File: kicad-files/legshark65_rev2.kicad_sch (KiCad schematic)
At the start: 206 parts, among them J1 ARM JTAG, J2 X1224WRS-04-LPV01, J3 Conn_01x04, SW1 K2-1187SQ-A4SW-06, SW2 PCM12SMTR, T2 SM04B-SRSS-TB, U1 STM32F411CEU6, U2 MCP1700T-3302E/TT, U3 AT24C256C-SSHL-T, Y1 TAXM8M4RFDCET2T

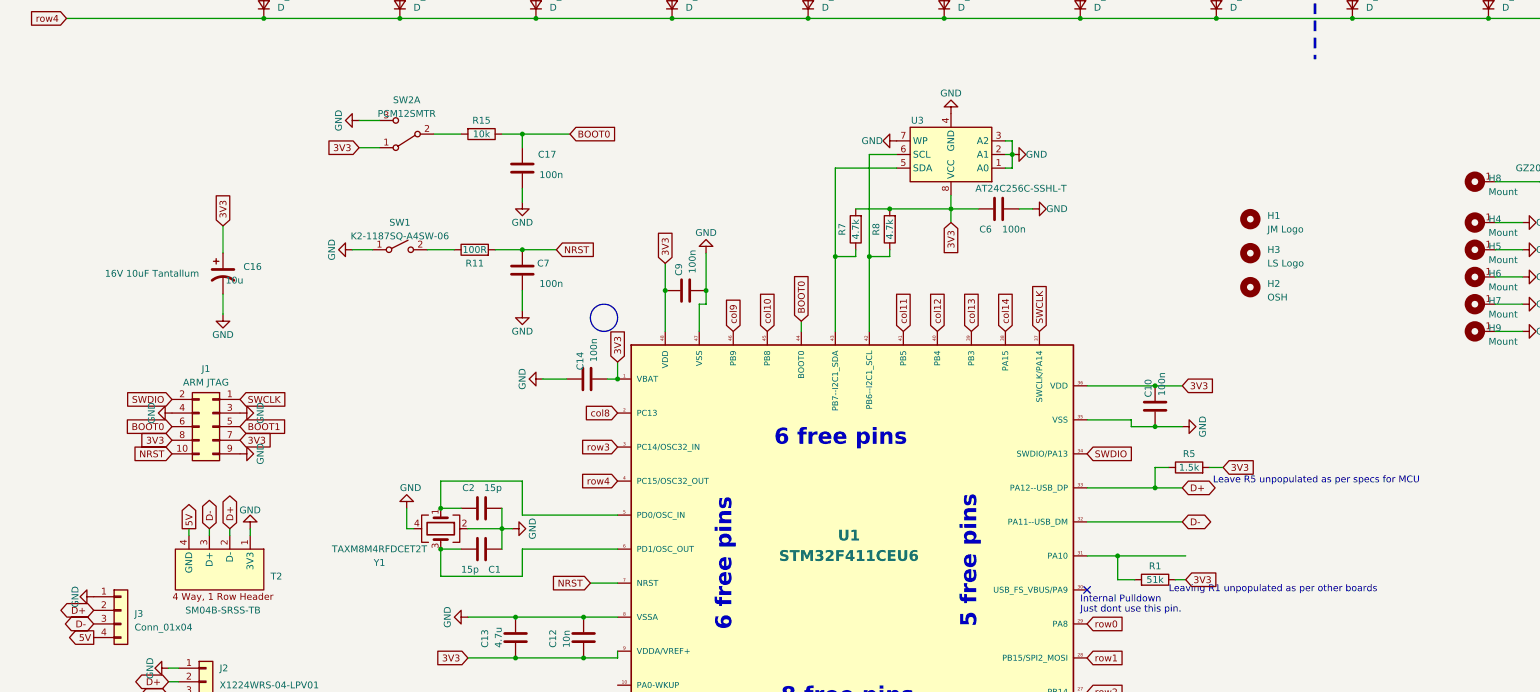
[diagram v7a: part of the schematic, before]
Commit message: Added power indicator LED
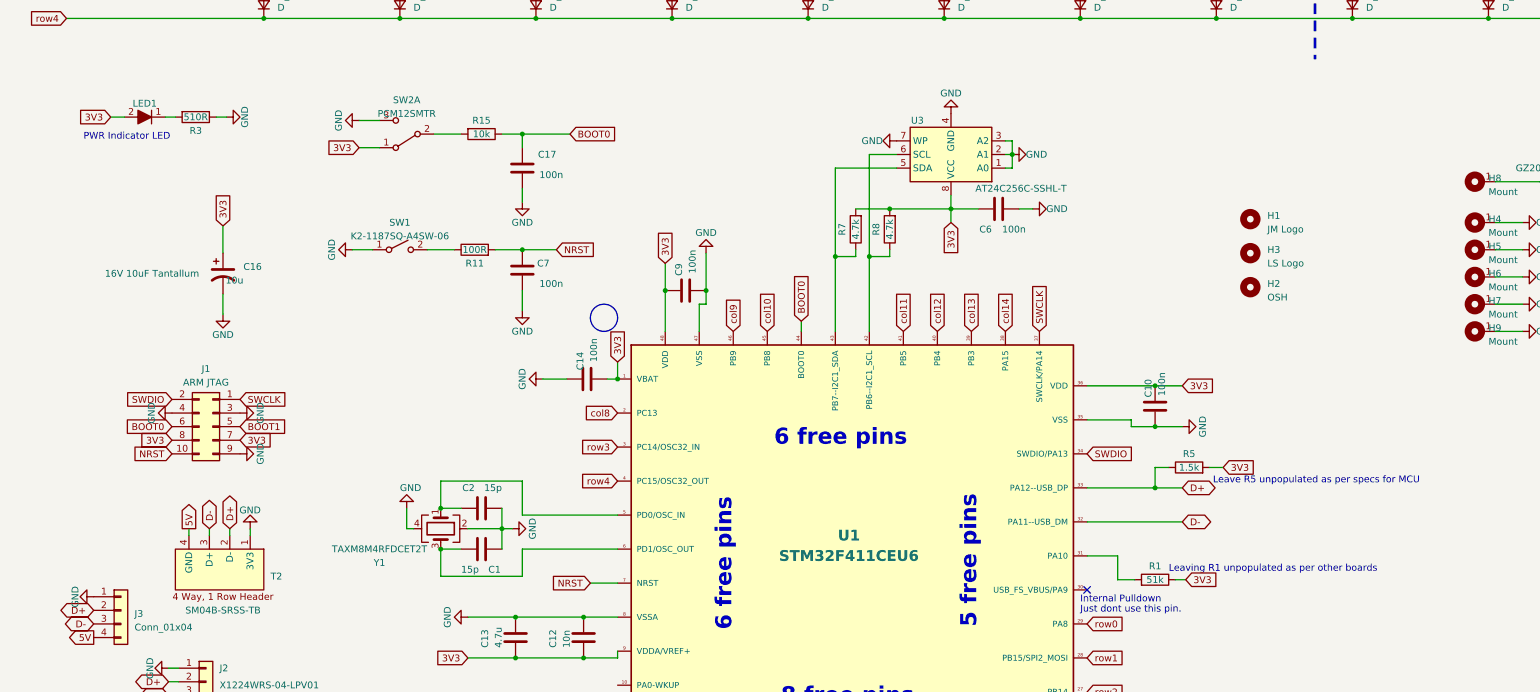
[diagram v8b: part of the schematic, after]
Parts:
- added LED1: ~, Legshark:LED_0603, symbol legshark_symbols:LED_0603
- added R3: 510R, Resistor_SMD:R_0402_1005Metric_Pad0.72x0.64mm_HandSolder, symbol Device:R
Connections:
- net 3V3: now also LED1.2
- net GND: now also R3.1
- new net: LED1.1, R3.2
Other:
- note added: "PWR Indicator LED"
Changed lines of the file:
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@@
   (junction (at 274.32 24.13) (diameter 0) (color 0 0 0 0)
   )
-  (junction (at 219.075 237.49) (diameter 0) (color 0 0 0 0)
-  )
   (junction (at 107.95 158.75) (diameter 0) (color 0 0 0 0)
   )
@@
     (stroke (width 0) (type default))
   )
-  (wire (pts (xy 219.075 237.49) (xy 231.775 237.49))
-    (stroke (width 0) (type default))
-  )
   (wire (pts (xy 135.89 111.76) (xy 161.29 111.76))
     (stroke (width 0) (type default))
@@
     (stroke (width 0) (type default))
   )
+  (wire (pts (xy 50.8 155.575) (xy 52.705 155.575))
+    (stroke (width 0) (type default))
+  )
   (wire (pts (xy 107.95 171.45) (xy 107.95 168.91))
     (stroke (width 0) (type default))
@@
     (stroke (width 0) (type default))
   )
+  (wire (pts (xy 31.115 155.575) (xy 33.655 155.575))
+    (stroke (width 0) (type default))
+  )
   (wire (pts (xy 299.72 100.33) (xy 299.72 74.93))
     (stroke (width 0) (type default))
@@
     (stroke (width 0) (type default))
   )
+  (wire (pts (xy 41.275 155.575) (xy 43.18 155.575))
+    (stroke (width 0) (type default))
+  )
   (wire (pts (xy 369.57 100.33) (xy 375.92 100.33))
     (stroke (width 0) (type default))
@@
     (effects (font (size 1.27 1.27)) (justify left bottom))
   )
+  (text "PWR Indicator LED" (at 26.035 160.02 0)
+    (effects (font (size 1.27 1.27)) (justify left bottom))
+  )
   (text "Leave R5 unpopulated as per specs for MCU" (at 236.855 224.155 0)
     (effects (font (size 1.27 1.27)) (justify left bottom))
@@
     (effects (font (size 1.27 1.27)) (justify left bottom))
   )
-  (text "Leaving R1 unpopulated as per other boards" (at 228.6 244.475 0)
+  (text "Leaving R1 unpopulated as per other boards" (at 228.6 240.665 0)
     (effects (font (size 1.27 1.27)) (justify left bottom))
   )
@@
     )
   )
+  (global_label "3V3" (shape input) (at 31.115 155.575 180) (fields_autoplaced)
+    (effects (font (size 1.27 1.27)) (justify right))
+    (property "Intersheetrefs" "${INTERSHEET_REFS}" (at 25.3558 155.575 0)
+      (effects (font (size 1.27 1.27)) (justify right) hide)
+    )
+  )
   (global_label "D-" (shape bidirectional) (at 41.91 263.525 180) (fields_autoplaced)
     (effects (font (size 1.27 1.27)) (justify right))
@@
     )
   )
+  (symbol (lib_id "legshark_symbols:LED_0603") (at 37.465 155.575 180) (unit 1)
+    (in_bom yes) (on_board yes) (dnp no)
+    (property "Reference" "LED1" (at 37.465 153.035 0)
+      (effects (font (size 1.27 1.27)))
+    )
+    (property "Value" "~" (at 38.735 156.845 0)
+      (effects (font (size 1.27 1.27)))
+    )
+    (property "Footprint" "Legshark:LED_0603" (at 38.735 156.845 0)
+      (effects (font (size 1.27 1.27)) hide)
+    )
+    (property "Datasheet" "" (at 38.735 156.845 0)
+      (effects (font (size 1.27 1.27)) hide)
+    )
+    (property "Specification" "Red 0603 SMD LED " (at 37.465 155.575 0)
+      (effects (font (size 1.27 1.27)) hide)
+    )
+    (pin "1")
+    (pin "2")
+    (instances
+      (project "legshark65_rev2"
+        (path "/2fcc1073-d3f4-43f9-b3b4-5cee13272705"
+          (reference "LED1") (unit 1)
+        )
+      )
+    )
+  )
   (symbol (lib_id "MX_Alps_Hybrid:MX-NoLED") (at 162.56 25.4 0) (unit 1)
     (in_bom yes) (on_board yes) (dnp no)
@@
     )
   )
+  (symbol (lib_id "power:GND") (at 52.705 155.575 90) (unit 1)
+    (in_bom yes) (on_board yes) (dnp no)
+    (property "Reference" "#PWR036" (at 59.055 155.575 0)
+      (effects (font (size 1.27 1.27)) hide)
+    )
+    (property "Value" "GND" (at 56.1547 153.5604 0)
+      (effects (font (size 1.27 1.27)) (justify right))
+    )
+    (property "Footprint" "" (at 52.705 155.575 0)
+      (effects (font (size 1.27 1.27)) hide)
+    )
+    (property "Datasheet" "" (at 52.705 155.575 0)
+      (effects (font (size 1.27 1.27)) hide)
+    )
+    (pin "1")
+    (instances
+      (project "legshark65_rev2"
+        (path "/2fcc1073-d3f4-43f9-b3b4-5cee13272705"
+          (reference "#PWR036") (unit 1)
+        )
+      )
+      (project "old_layout"
+        (path "/2fda2561-53ed-4930-8b41-858e0e3dd5f4"
+          (reference "#PWR031") (unit 1)
+        )
+      )
+      (project "legshark65_rev1"
+        (path "/9ddf6dc5-8b5e-413a-9b25-d1d5a5a60469"
+          (reference "#PWR02") (unit 1)
+        )
+      )
+    )
+  )
   (symbol (lib_id "Device:R") (at 92.71 294.64 180) (unit 1)
     (in_bom yes) (on_board yes) (dnp no)
@@
         )
       )
+    )
+  )
+  (symbol (lib_id "Device:R") (at 46.99 155.575 270) (unit 1)
+    (in_bom yes) (on_board yes) (dnp no)
+    (property "Reference" "R3" (at 46.99 158.115 90)
+      (effects (font (size 1.27 1.27)))
+    )
+    (property "Value" "510R" (at 46.99 155.575 90)
+      (effects (font (size 1.27 1.27)))
+    )
+    (property "Footprint" "Resistor_SMD:R_0402_1005Metric_Pad0.72x0.64mm_HandSolder" (at 46.99 153.797 90)
+      (effects (font (size 1.27 1.27)) hide)
+    )
+    (property "Datasheet" "~" (at 46.99 155.575 0)
+      (effects (font (size 1.27 1.27)) hide)
+    )
+    (property "LCSC Part" "C23162" (at 46.99 155.575 0)
+      (effects (font (size 1.27 1.27)) hide)
+    )
+    (property "Manufacturer" "Uniroyal Elec" (at 46.99 155.575 0)
+      (effects (font (size 1.27 1.27)) hide)
+    )
+    (property "Manufacturer Part Number" "0603WAF4701T5E" (at 46.99 155.575 0)
+      (effects (font (size 1.27 1.27)) hide)
+    )
+    (property "Package" "0603" (at 46.99 155.575 0)
+      (effects (font (size 1.27 1.27)) hide)
+    )
+    (property "Specification" "±1% 4.7kΩ 0603 Chip Resistor" (at 46.99 155.575 0)
+      (effects (font (size 1.27 1.27)) hide)
+    )
+    (property "Vendor Part Number" "LCSC C23162" (at 46.99 155.575 0)
+      (effects (font (size 1.27 1.27)) hide)
+    )
+    (pin "1")
+    (pin "2")
+    (instances
+      (project "legshark65_rev2"
+        (path "/2fcc1073-d3f4-43f9-b3b4-5cee13272705"
+          (reference "R3") (unit 1)
+        )
+      )
+      (project "old_layout"
+        (path "/2fda2561-53ed-4930-8b41-858e0e3dd5f4"
+          (reference "R7") (unit 1)
+        )
+      )
+      (project "legshark65_rev1"
+        (path "/9ddf6dc5-8b5e-413a-9b25-d1d5a5a60469"
+          (reference "R7") (unit 1)
+        )
+      )
